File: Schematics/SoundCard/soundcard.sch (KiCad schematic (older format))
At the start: 8 parts, among them J1 Conn_01x09_Female, U1 LM386

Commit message: Save all Schematics again to overcome problems with version change
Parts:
- J1: symbol Connector:Conn_01x11_Female -> Connector:Conn_01x12_Female
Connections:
- net at A1.10 (D7): now also J1.7 (Pin_7); no longer J1.6 (Pin_6)
- net at A1.11 (D8): now also J1.8 (Pin_8); no longer J1.7 (Pin_7)
- net at A1.12 (D9): now also J1.9 (Pin_9); no longer J1.8 (Pin_8)
- net at A1.13 (D10): now also J1.10 (Pin_10); no longer J1.9 (Pin_9)
- net at A1.14 (D11): now also J1.11 (Pin_11); no longer J1.10 (Pin_10)
- net at A1.15 (D12): now also J1.12 (Pin_12); no longer J1.11 (Pin_11)
- net at A1.6 (D3): now also J1.3 (Pin_3)
- net at A1.7 (D4): now also J1.4 (Pin_4); no longer J1.3 (Pin_3)
- net at A1.8 (D5): now also J1.5 (Pin_5); no longer J1.4 (Pin_4)
- net at A1.9 (D6): now also J1.6 (Pin_6); no longer J1.5 (Pin_5)
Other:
- note added: "5V"
- note added: "D0"
- note added: "D1"
- note added: "D2"
- note added: "D3"
- note added: "D4"
- note added: "D5"
- note added: "D6"
- note added: "D7"
- note added: "GND"
- note added: "SOUND_~CS"
- note added: "Z80_~WR"
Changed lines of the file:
@@
 $EndComp
 $Comp
-L Connector:Conn_01x11_Female J1
+L Connector:Conn_01x12_Female J1
 U 1 1 5C467285
-P 3900 3750
-F 0 "J1" H 3750 3150 50  0000 L CNN
-F 1 "Conn_01x09_Female" H 3450 3250 50  0001 L CNN
-F 2 "" H 3900 3750 50  0001 C CNN
-F 3 "~" H 3900 3750 50  0001 C CNN
-	1    3900 3750
+P 3800 3650
+F 0 "J1" H 3650 3000 50  0000 L CNN
+F 1 "Conn_01x09_Female" H 3350 3150 50  0001 L CNN
+F 2 "" H 3800 3650 50  0001 C CNN
+F 3 "~" H 3800 3650 50  0001 C CNN
+	1    3800 3650
 	-1   0    0    -1
 $EndComp
@@
 Wire Wire Line
 	5000 2550 4100 2550
-Wire Wire Line
-	4100 2550 4100 3250
-Wire Wire Line
-	4100 3350 4250 3350
-Wire Wire Line
-	4250 3350 4250 2600
-Wire Wire Line
-	4250 2600 5400 2600
 Wire Wire Line
 	5400 2600 5400 4650
@@
 	5400 4650 4900 4650
 Connection ~ 4900 4650
-Wire Wire Line
-	4100 3450 4300 3450
-Wire Wire Line
-	4100 3550 4300 3550
-Wire Wire Line
-	4100 3650 4300 3650
-Wire Wire Line
-	4100 3750 4300 3750
-Wire Wire Line
-	4100 3850 4300 3850
-Wire Wire Line
-	4100 3950 4300 3950
-Wire Wire Line
-	4100 4050 4300 4050
-Wire Wire Line
-	4100 4150 4300 4150
-Wire Wire Line
-	4100 4250 4300 4250
-Text Label 3800 3450 3    100  ~ 0
-Data_Bus
 $Comp
 L Amplifier_Audio:LM386 U1
@@
 Wire Wire Line
 	4150 4350 4300 4350
+Wire Wire Line
+	4000 4250 4300 4250
+Wire Wire Line
+	4000 4150 4300 4150
+Wire Wire Line
+	4000 4050 4300 4050
+Wire Wire Line
+	4000 3950 4300 3950
+Wire Wire Line
+	4000 3850 4300 3850
+Wire Wire Line
+	4000 3750 4300 3750
+Wire Wire Line
+	4000 3650 4300 3650
+Wire Wire Line
+	4000 3550 4300 3550
+Wire Wire Line
+	4000 3450 4300 3450
+Wire Wire Line
+	4000 3350 4300 3350
+Wire Wire Line
+	4000 3150 4100 3150
+Wire Wire Line
+	4100 3150 4100 2550
+Wire Wire Line
+	4150 2600 4150 3250
+Wire Wire Line
+	4150 3250 4000 3250
+Wire Wire Line
+	4150 2600 5400 2600
+Text Notes 3650 3200 0    50   ~ 0
+5V
+Text Notes 3600 3300 0    50   ~ 0
+GND
+Text Notes 3350 3400 0    50   ~ 0
+SOUND_~CS
+Text Notes 3450 3500 0    50   ~ 0
+Z80_~WR
+Text Notes 3650 3600 0    50   ~ 0
+D7
+Text Notes 3650 3700 0    50   ~ 0
+D6
+Text Notes 3650 3800 0    50   ~ 0
+D5
+Text Notes 3650 3900 0    50   ~ 0
+D4
+Text Notes 3650 4000 0    50   ~ 0
+D3
+Text Notes 3650 4100 0    50   ~ 0
+D2
+Text Notes 3650 4200 0    50   ~ 0
+D1
+Text Notes 3650 4300 0    50   ~ 0
+D0
 $EndSCHEMATC

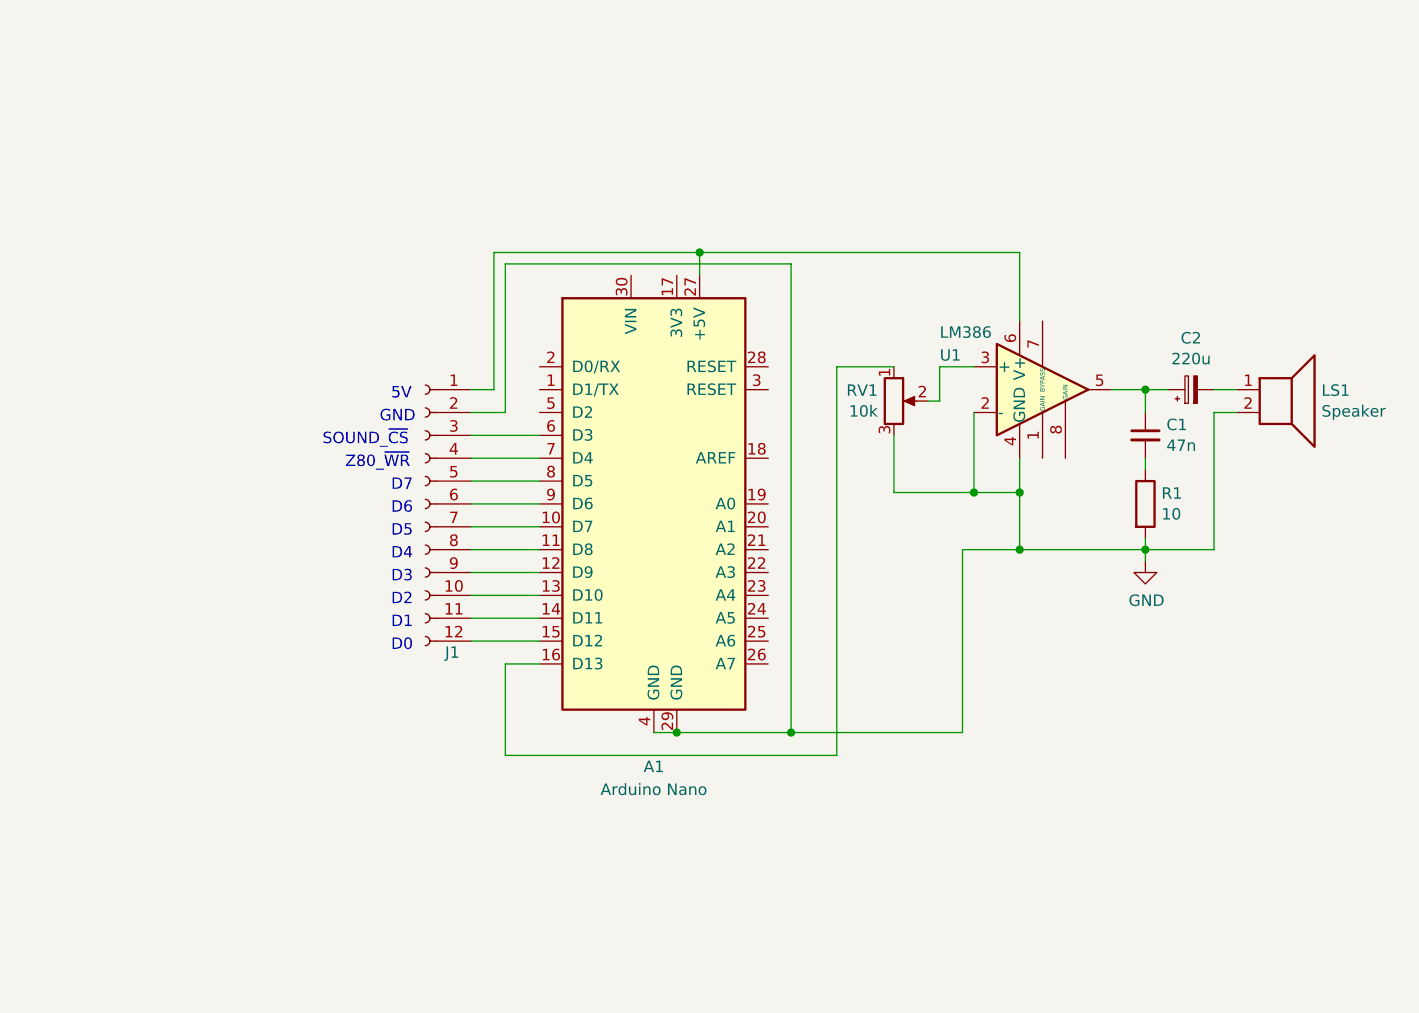
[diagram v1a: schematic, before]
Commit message: Redesign the sound card to use a bare Atmega 328P instead of arduino nano
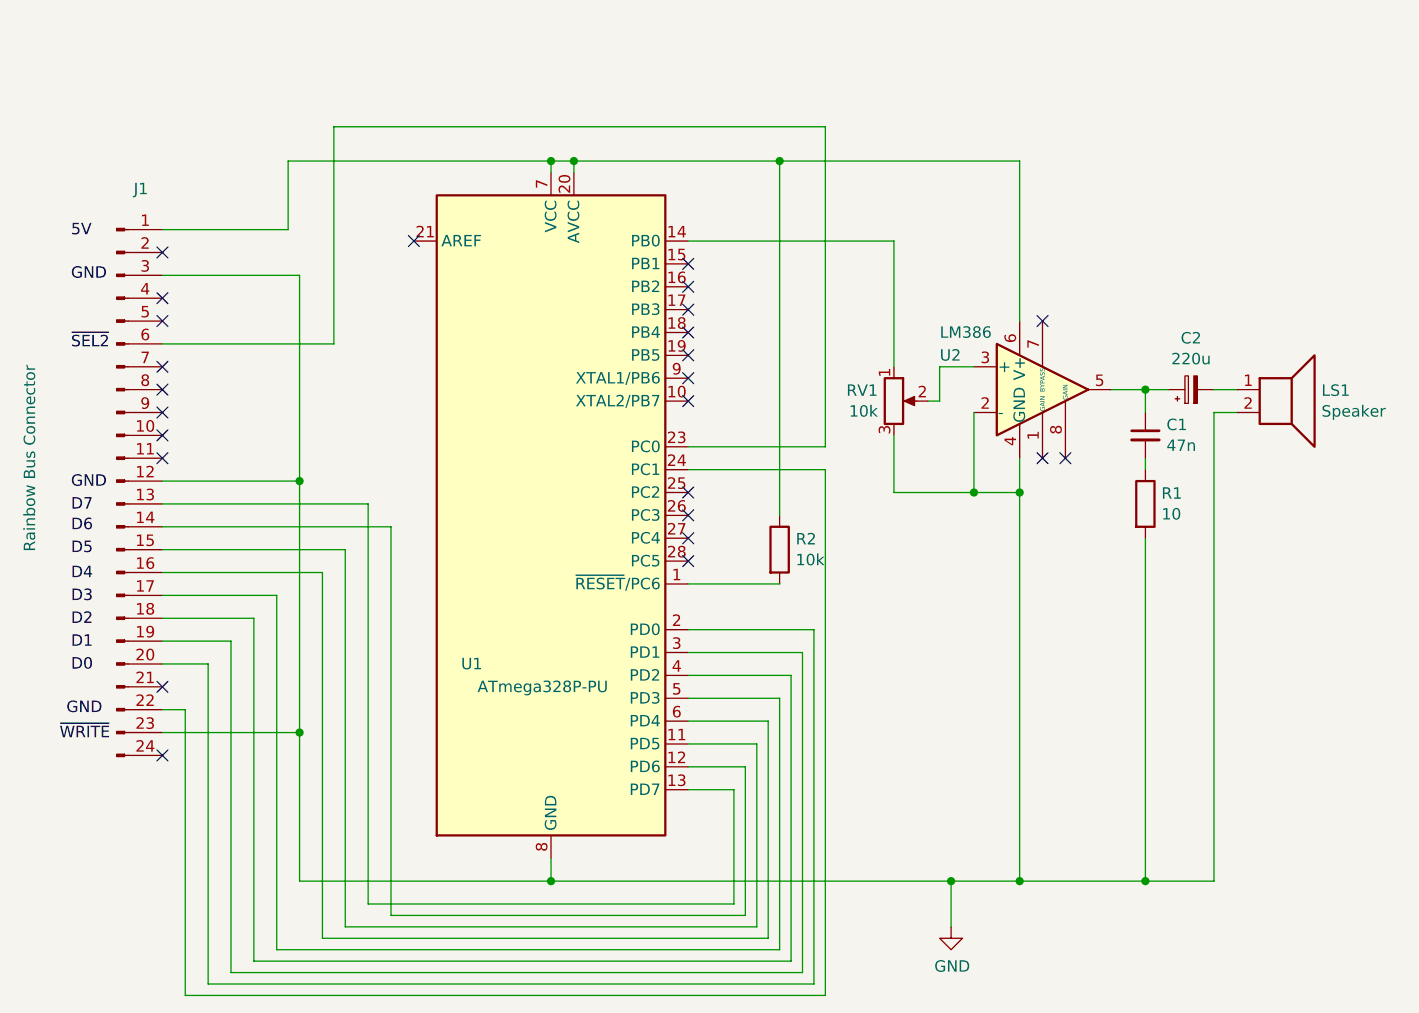
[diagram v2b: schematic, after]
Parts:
- removed A1: Arduino Nano, Module:Arduino_Nano, symbol MCU_Module:Arduino_Nano_v3.x
- removed J1: Conn_01x09_Female, symbol Connector:Conn_01x12_Female
- added J1: Rainbow Bus Connector, symbol Connector:Conn_01x24_Male
- added R2: 10k, symbol Device:R
- added U1: ATmega328P-PU, Package_DIP:DIP-28_W7.62mm, symbol MCU_Microchip_ATmega:ATmega328P-PU
- renumbered U1 to U2
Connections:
- net GND: now also J1.12 (Pin_12), J1.23 (Pin_23), J1.3 (Pin_3), U1.22 (GND), U1.8 (GND)
- net at RV1.1: now also U1.14 (PB0)
- net at U2.6 (V+): now also J1.1 (Pin_1), R2.1, U1.20 (AVCC), U1.7 (VCC)
- new net: R2.2, U1.1 (~RESET~/PC6)
- new net: J1.15 (Pin_15), U1.11 (PD5)
- new net: J1.14 (Pin_14), U1.12 (PD6)
- new net: J1.13 (Pin_13), U1.13 (PD7)
- new net: J1.20 (Pin_20), U1.2 (PD0)
- new net: J1.6 (Pin_6), U1.23 (PC0)
- new net: J1.22 (Pin_22), U1.24 (PC1)
- new net: J1.19 (Pin_19), U1.3 (PD1)
- new net: J1.18 (Pin_18), U1.4 (PD2)
- new net: J1.17 (Pin_17), U1.5 (PD3)
- new net: J1.16 (Pin_16), U1.6 (PD4)
- no-connect marks 0 -> 25
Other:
- note removed: "5V"
- note removed: "D0"
- note removed: "D1"
- note removed: "D2"
- note removed: "D3"
- note removed: "D4"
- note removed: "D5"
- note removed: "D6"
- note removed: "D7"
- note removed: "GND"
- note removed: "SOUND_~CS"
- note removed: "Z80_~WR"

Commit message: Add power flags to sound card schematic
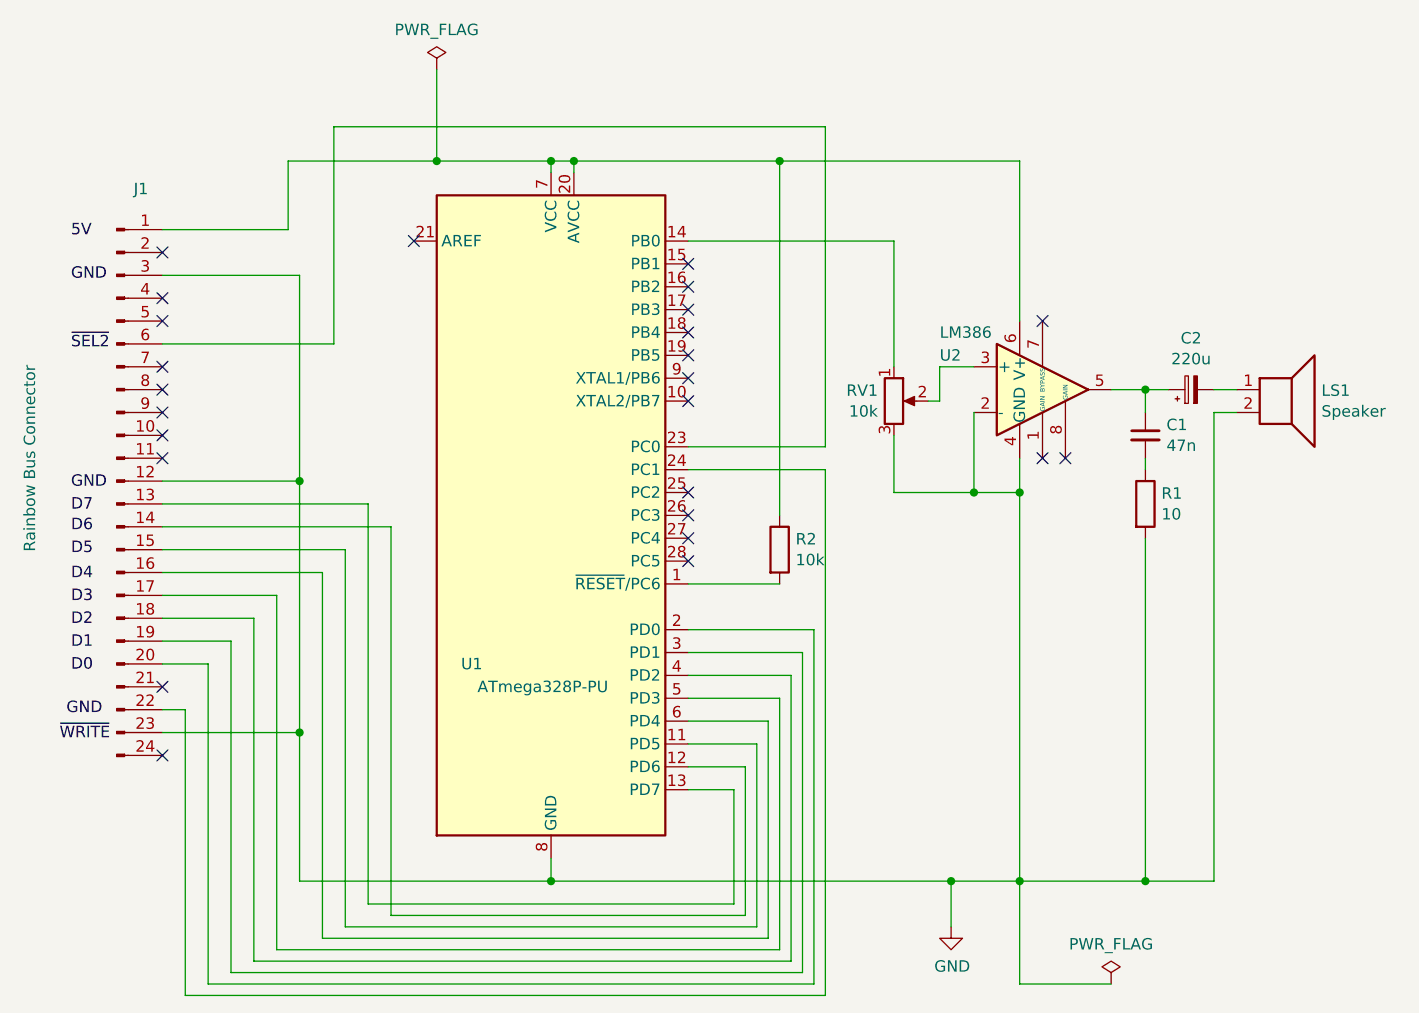
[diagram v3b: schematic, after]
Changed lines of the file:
@@
 	4350 2200 4350 2150
 Wire Wire Line
-	4350 2150 3200 2150
+	4350 2150 3850 2150
 Wire Wire Line
 	3200 2150 3200 2450
@@
 Text Label 2200 4690 0    50   ~ 0
 ~WRITE
+$Comp
+L power:PWR_FLAG #FLG?
+U 1 1 5C89360F
+P 6800 5750
+F 0 "#FLG?" H 6800 5825 50  0001 C CNN
+F 1 "PWR_FLAG" H 6800 5924 50  0000 C CNN
+F 2 "" H 6800 5750 50  0001 C CNN
+F 3 "~" H 6800 5750 50  0001 C CNN
+	1    6800 5750
+	1    0    0    -1
+$EndComp
+Wire Wire Line
+	6800 5750 6400 5750
+Wire Wire Line
+	6400 5750 6400 5300
+$Comp
+L power:PWR_FLAG #FLG?
+U 1 1 5C8962B8
+P 3850 1750
+F 0 "#FLG?" H 3850 1825 50  0001 C CNN
+F 1 "PWR_FLAG" H 3850 1924 50  0000 C CNN
+F 2 "" H 3850 1750 50  0001 C CNN
+F 3 "~" H 3850 1750 50  0001 C CNN
+	1    3850 1750
+	1    0    0    -1
+$EndComp
+Wire Wire Line
+	3850 1750 3850 2150
+Connection ~ 3850 2150
+Wire Wire Line
+	3850 2150 3200 2150
 $EndSCHEMATC
